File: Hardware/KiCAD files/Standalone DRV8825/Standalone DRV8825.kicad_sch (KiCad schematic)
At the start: 18 parts, among them J10 PINHD_1x8_Male, J9 PINHD_1x8_Male, U5 DRV8825PWPR

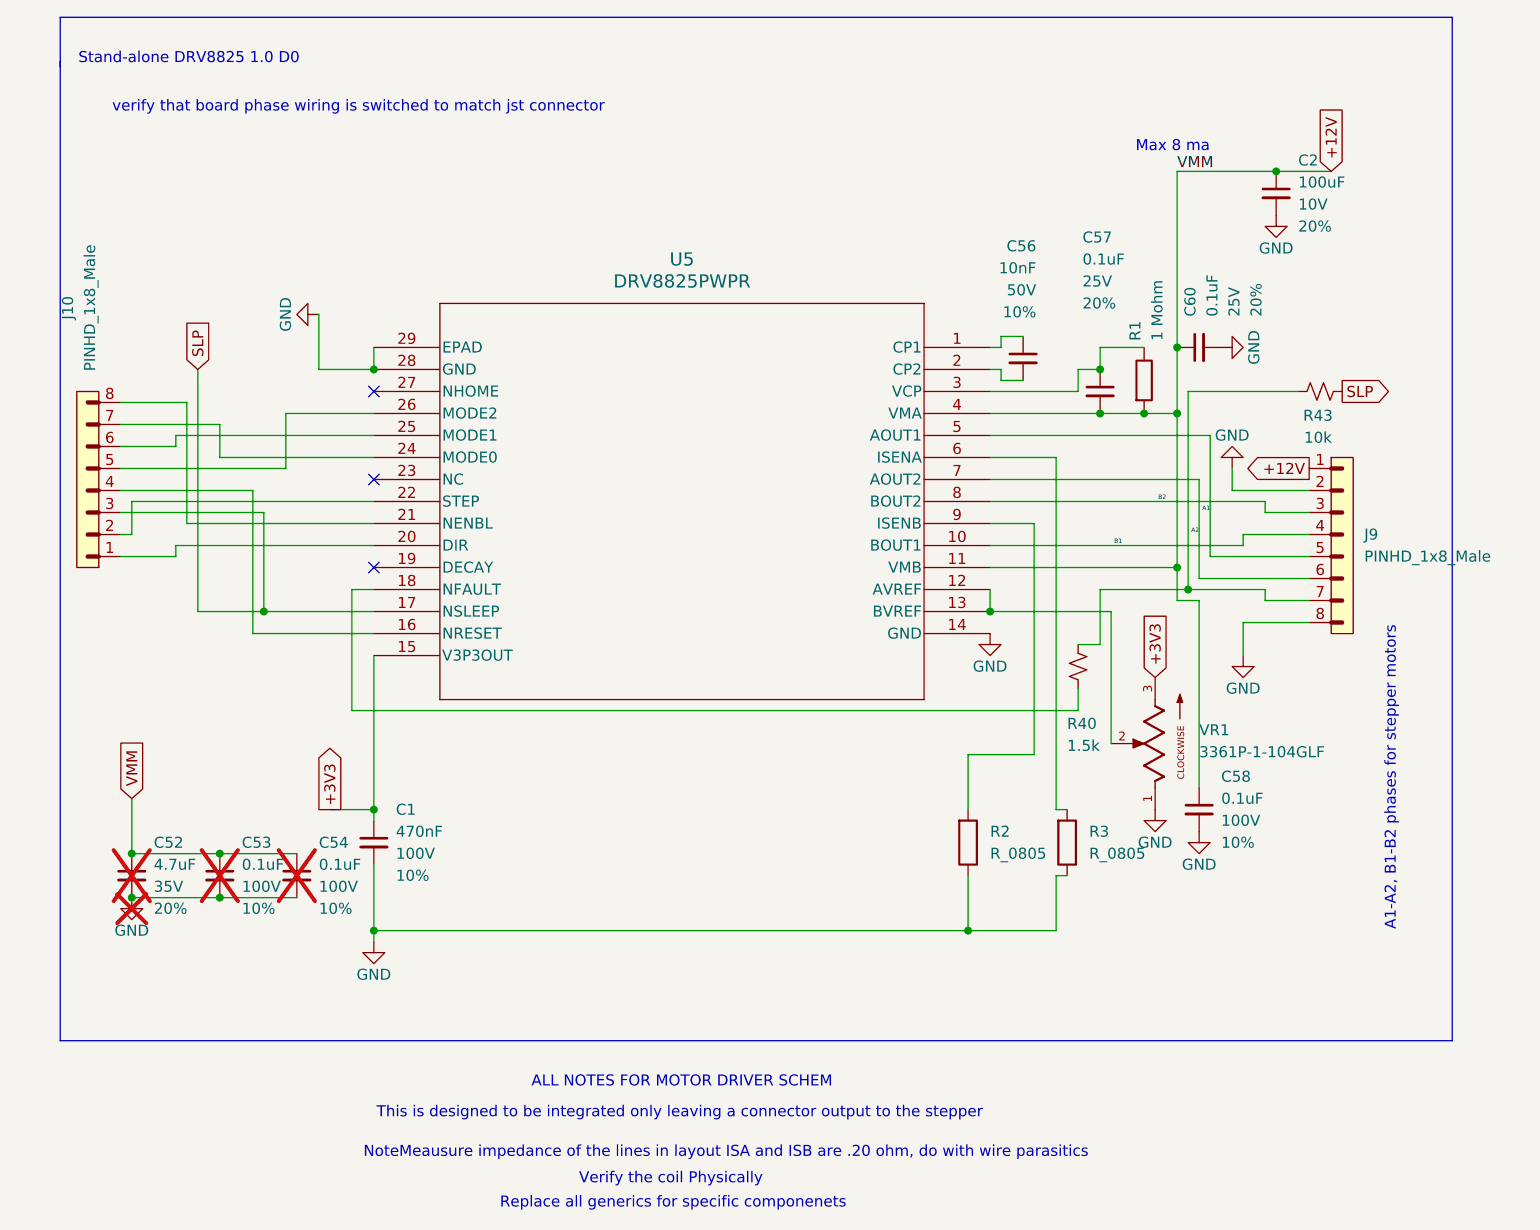
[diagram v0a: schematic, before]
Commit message: general progress and adjustments
new footprint for pi reg inductor, var reg checked concurred with current part and value. re footprinted motor driver. started swapping head. adjusted some device footprints.
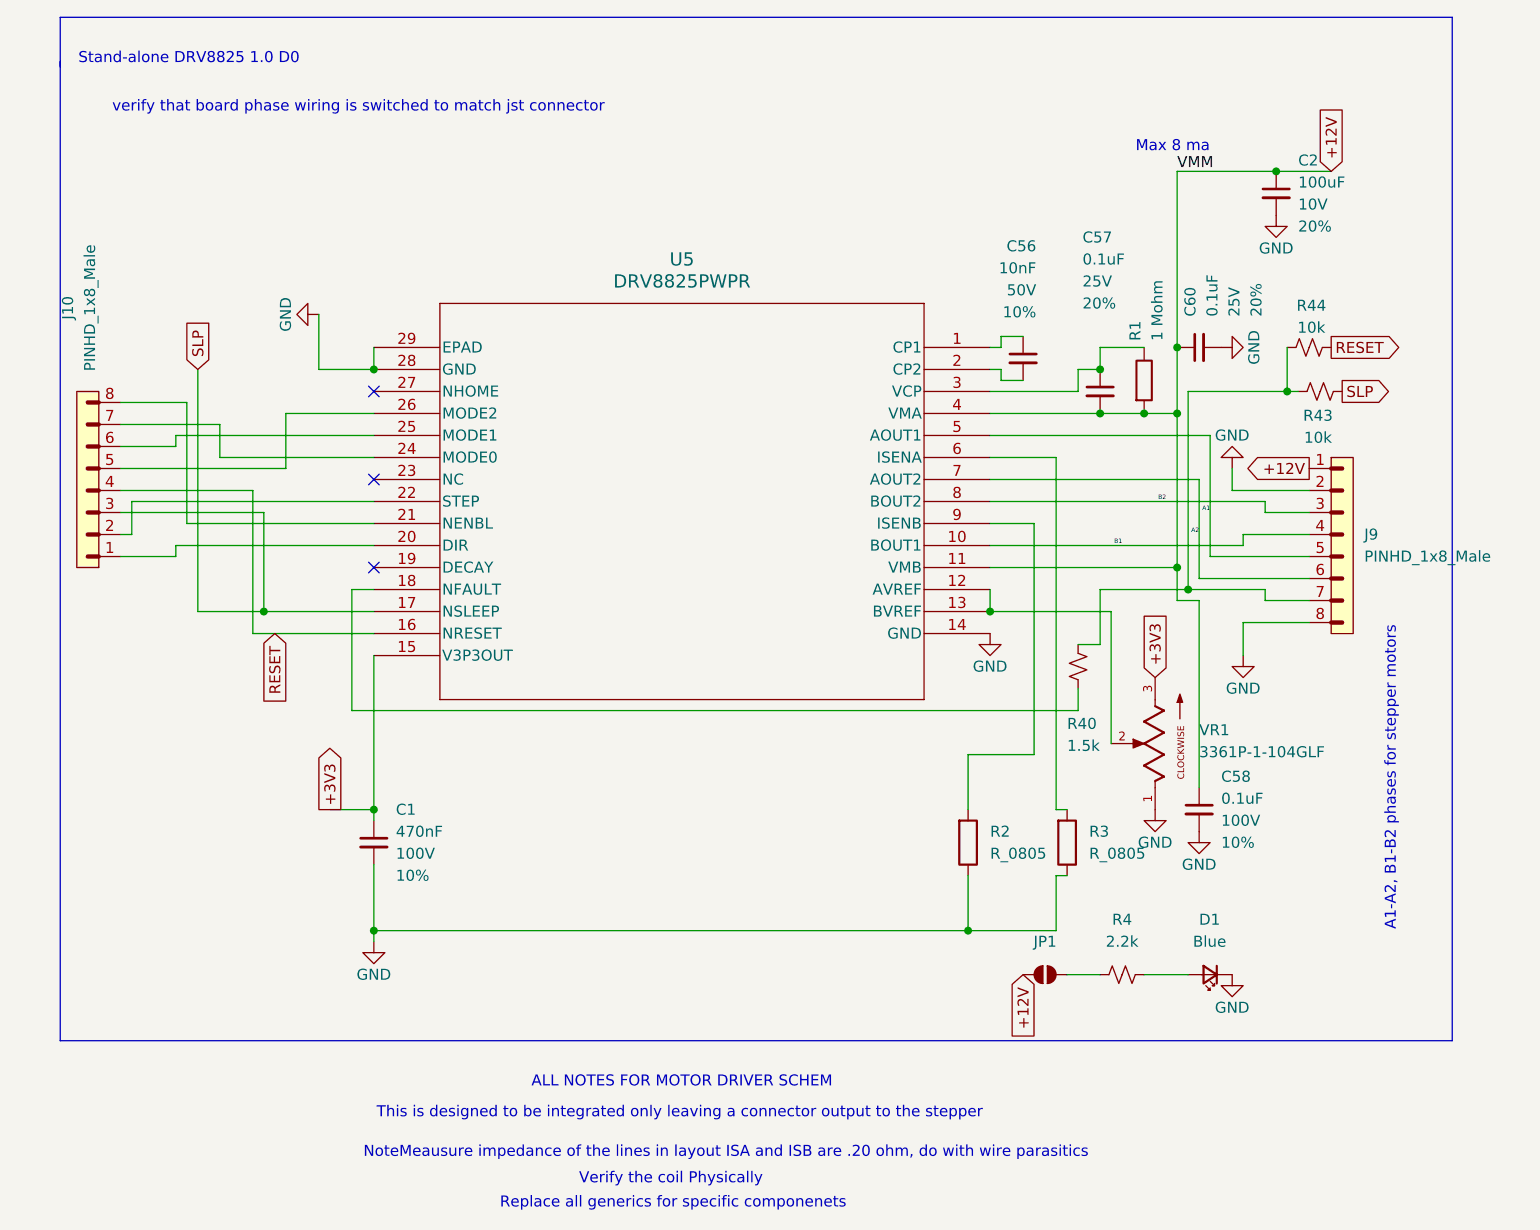
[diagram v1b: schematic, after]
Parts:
- removed C52: 4.7uF, PCM_SparkFun-Capacitor:C_0603_1608Metric, symbol PCM_SparkFun-Capacitor:4.7uF_0603_35V_20%
- removed C53, C54: 0.1uF, PCM_SparkFun-Capacitor:C_0603_1608Metric, symbol PCM_SparkFun-Capacitor:0.1uF_0603_100V_10%
- added D1: Blue, PCM_SparkFun-LED:LED_0603_1608Metric_Blue, symbol PCM_SparkFun-LED:LED_Blue_0603
- added JP1: (no value), PCM_SparkFun-Jumper:Jumper_2_NO, symbol PCM_SparkFun-Jumper:SolderJumper_2_Open
- added R4: 2.2k, PCM_SparkFun-Resistor:R_0603_1608Metric, symbol PCM_SparkFun-Resistor:2.2k_0603
- added R44: 10k, PCM_SparkFun-Resistor:R_0603_1608Metric, symbol PCM_SparkFun-Resistor:10k_0603
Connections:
- net +12V: now also JP1.1 (A)
- net GND: now also D1.1 (K)
- net RESET: now reaches J10.4, U5.16 (NRESET)
- net RESET: now also R44.2
- net at J9.7, R40.2, R43.1: now also R44.1
- new net: JP1.2 (B), R4.1
- new net: D1.2 (A), R4.2

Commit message: general updates to the schematics and layouts
includes some backchecks tot he master schematic to be accurate for the paper
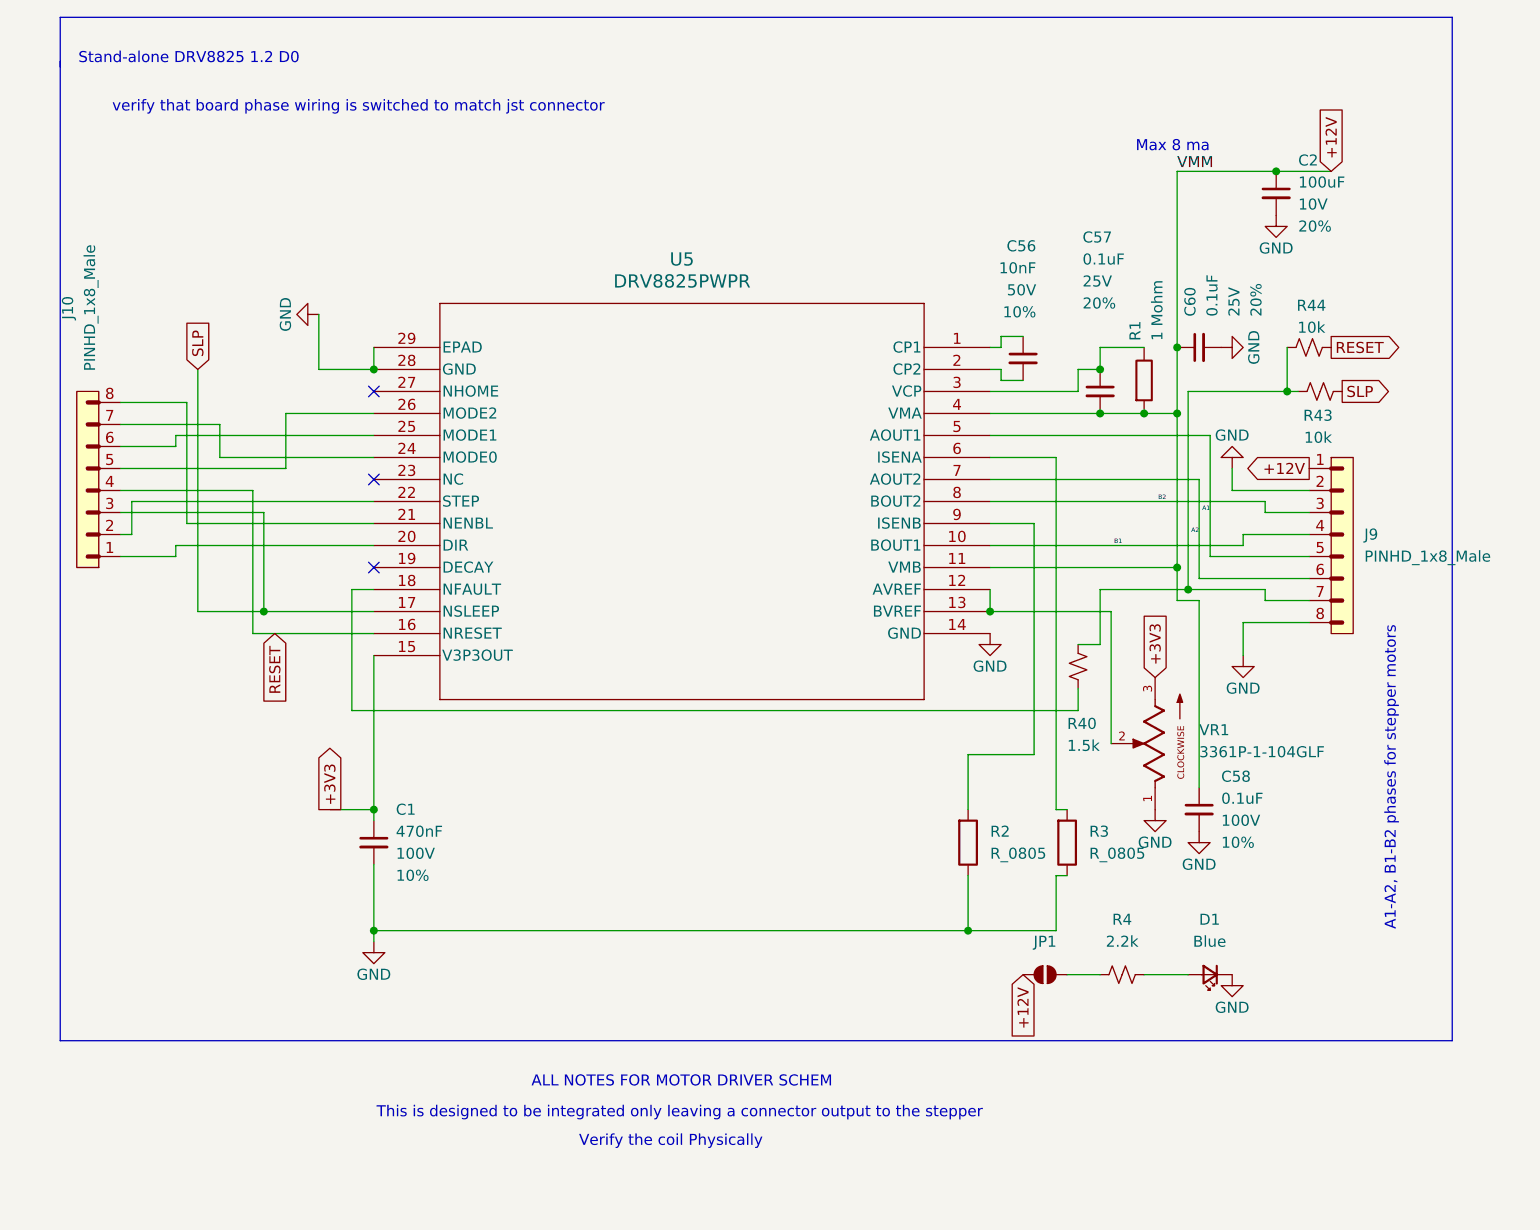
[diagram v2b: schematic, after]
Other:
- note added: "Stand-alone DRV8825 1.2 D0"
- note removed: "NoteMeausure impedance of the lines in layout ISA and ISB are .20 ohm, do with wire parasitics"
- note removed: "Replace all generics for specific componenets"
- note removed: "Stand-alone DRV8825 1.0 D0"
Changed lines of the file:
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@@
 	(generator_version "10.0")
 	(paper "A4")
-	(text "NoteMeausure impedance of the lines in layout ISA and ISB are .20 ohm, do with wire parasitics"
-		(exclude_from_sim no)
-		(at 146.05 148.844 0)
-		(effects
-			(font
-				(size 1.27 1.27)
-			)
-		)
-	)
 	(text "This is designed to be integrated only leaving a connector output to the stepper"
 		(exclude_from_sim no)
@@
 		(exclude_from_sim no)
 		(at 140.97 140.716 0)
-		(effects
-			(font
-				(size 1.27 1.27)
-			)
-		)
-	)
-	(text "Replace all generics for specific componenets\n"
-		(exclude_from_sim no)
-		(at 139.954 154.686 0)
 		(effects
 			(font
@@
 		)
 	)
-	(text "Stand-alone DRV8825 1.0 D0"
+	(text "Stand-alone DRV8825 1.2 D0"
 		(exclude_from_sim no)
 		(at 84.074 22.606 0)
@@
 	(text "Verify the coil Physically"
 		(exclude_from_sim no)
-		(at 139.7 151.892 0)
+		(at 139.7 147.574 0)
 		(effects
 			(font

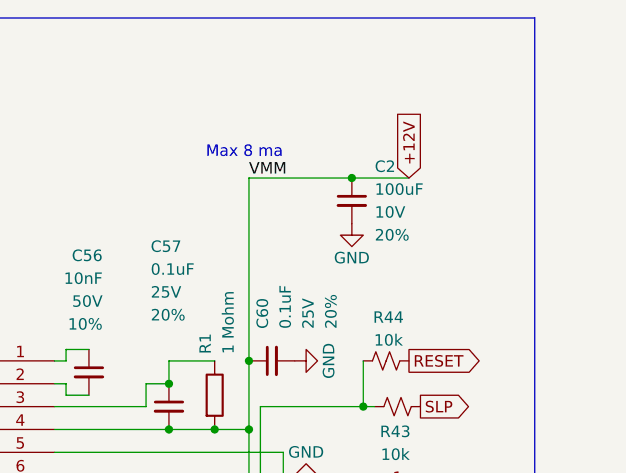
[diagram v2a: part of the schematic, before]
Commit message: part of the way through next iteration
Non-daisy chain Mainboard is ~50% through
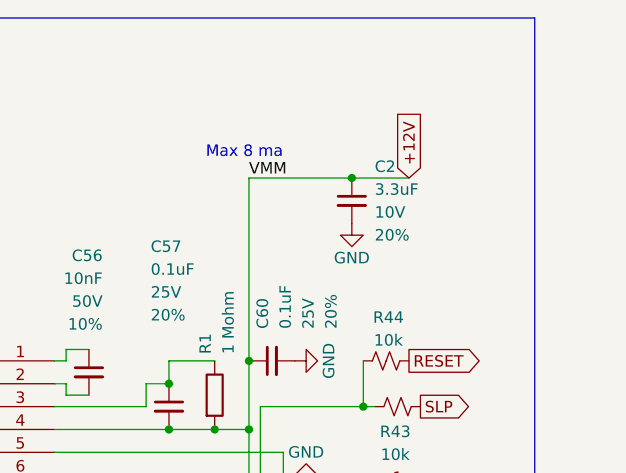
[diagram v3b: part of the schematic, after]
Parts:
- C2: value 100uF -> 3.3uF
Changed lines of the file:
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@@
 			)
 		)
-		(property "Value" "100uF"
+		(property "Value" "3.3uF"
 			(at 212.09 36.8362 0)
 			(show_name no)

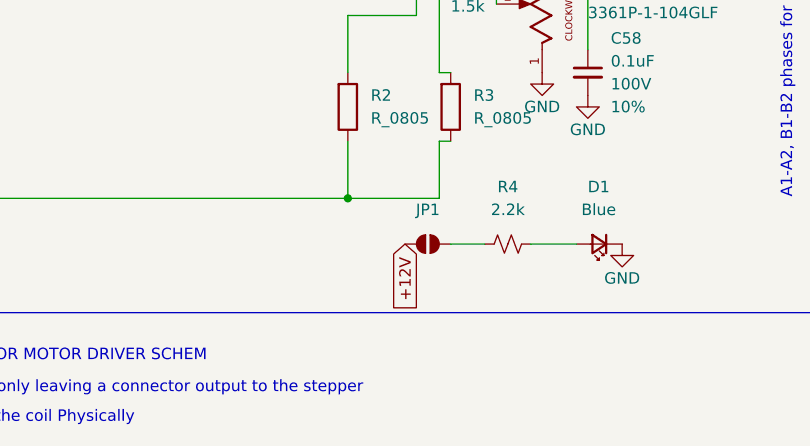
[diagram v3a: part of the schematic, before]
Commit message: 1st submitted iteration
added a folder for reviewing PCB's.
fixed various smaller issues on the PCB.
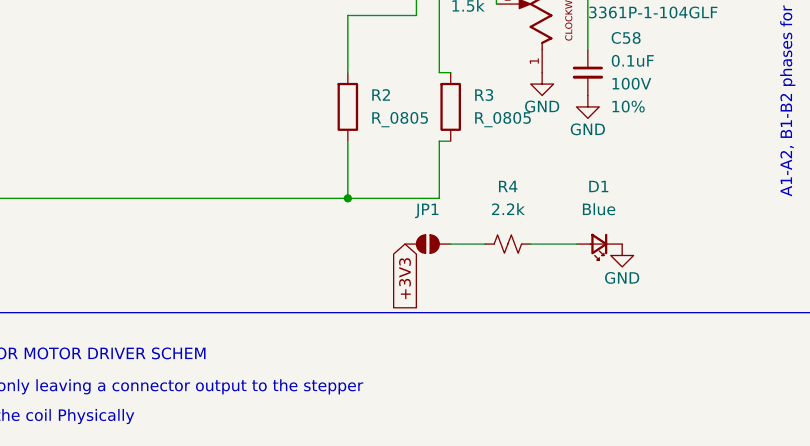
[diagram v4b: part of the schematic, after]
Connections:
- net +12V: no longer JP1.1 (A)
- net +3V3: now also JP1.1 (A)
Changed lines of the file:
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@@
 		)
 	)
-	(global_label "+12V"
+	(global_label "+3V3"
 		(shape input)
 		(at 180.34 128.27 270)

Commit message: sick weekend changes
small adjustments left our some larger protection changes till after talking to weeks
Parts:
- removed JP1: (no value), PCM_SparkFun-Jumper:Jumper_2_NO, symbol PCM_SparkFun-Jumper:SolderJumper_2_Open
- added R5: 0, Resistor_SMD:R_0805_2012Metric, symbol PCM_SparkFun-Resistor:2.2k_0603
- R4: footprint PCM_SparkFun-Resistor:R_0603_1608Metric -> Resistor_SMD:R_0805_2012Metric
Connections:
- net +3V3: now also R5.1
- net at R4.1: now also R5.2
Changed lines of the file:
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@@
 			)
 		)
-		(property "Footprint" "PCM_SparkFun-Resistor:R_0603_1608Metric"
+		(property "Footprint" "Resistor_SMD:R_0805_2012Metric"
 			(at 191.77 132.588 0)
 			(hide yes)
@@
 	)
 	(symbol
-		(lib_id "PCM_SparkFun-Jumper:SolderJumper_2_Open")
-		(at 182.88 128.27 0)
-		(unit 1)
-		(body_style 1)
-		(exclude_from_sim no)
-		(in_bom yes)
-		(on_board yes)
-		(in_pos_files yes)
-		(dnp no)
-		(fields_autoplaced yes)
-		(property "Reference" "JP1"
-			(at 182.88 124.46 0)
-			(show_name no)
-			(do_not_autoplace no)
-			(effects
-				(font
-					(size 1.27 1.27)
-				)
-			)
-		)
-		(property "Value" ""
-			(at 182.88 130.81 0)
-			(show_name no)
-			(do_not_autoplace no)
-			(effects
-				(font
-					(size 1.27 1.27)
-				)
-			)
-		)
-		(property "Footprint" "PCM_SparkFun-Jumper:Jumper_2_NO"
-			(at 182.88 131.572 0)
-			(hide yes)
-			(show_name no)
-			(do_not_autoplace no)
-			(effects
-				(font
-					(size 1.27 1.27)
-				)
-			)
-		)
-		(property "Datasheet" ""
-			(at 182.88 134.62 0)
-			(hide yes)
-			(show_name no)
-			(do_not_autoplace no)
-			(effects
-				(font
-					(size 1.27 1.27)
-				)
-			)
-		)
-		(property "Description" "Solder Jumper, 2-pole, open"
-			(at 182.88 137.16 0)
-			(hide yes)
-			(show_name no)
-			(do_not_autoplace no)
-			(effects
-				(font
-					(size 1.27 1.27)
-				)
-			)
-		)
-		(pin "1"
-		)
-		(pin "2"
-		)
-		(instances
-			(project "Standalone DRV8825"
-				(path "/f9c8590d-b7bb-4825-888e-ef9187573820"
-					(reference "JP1")
-					(unit 1)
-				)
-			)
-		)
-	)
-	(symbol
 		(lib_id "PCM_SparkFun-Capacitor:0.1uF_0603_100V_10%")
 		(at 200.66 109.22 0)
@@
 					(unit 1)
 				)
+			)
+		)
+	)
+	(symbol
+		(lib_id "PCM_SparkFun-Resistor:2.2k_0603")
+		(at 182.88 128.27 0)
+		(unit 1)
+		(body_style 1)
+		(exclude_from_sim no)
+		(in_bom yes)
+		(on_board yes)
+		(in_pos_files yes)
+		(dnp no)
+		(fields_autoplaced yes)
+		(property "Reference" "R5"
+			(at 182.88 121.92 0)
+			(show_name no)
+			(do_not_autoplace no)
+			(effects
+				(font
+					(size 1.27 1.27)
+				)
+			)
+		)
+		(property "Value" "0"
+			(at 182.88 124.46 0)
+			(show_name no)
+			(do_not_autoplace no)
+			(effects
+				(font
+					(size 1.27 1.27)
+				)
+			)
+		)
+		(property "Footprint" "Resistor_SMD:R_0805_2012Metric"
+			(at 182.88 132.588 0)
+			(hide yes)
+			(show_name no)
+			(do_not_autoplace no)
+			(effects
+				(font
+					(size 1.27 1.27)
+				)
+			)
+		)
+		(property "Datasheet" "https://www.vishay.com/docs/20035/dcrcwe3.pdf"
+			(at 182.88 137.16 0)
+			(hide yes)
+			(show_name no)
+			(do_not_autoplace no)
+			(effects
+				(font
+					(size 1.27 1.27)
+				)
+			)
+		)
+		(property "Description" "Resistor"
+			(at 182.88 139.7 0)
+			(hide yes)
+			(show_name no)
+			(do_not_autoplace no)
+			(effects
+				(font
+					(size 1.27 1.27)
+				)
+			)
+		)
+		(property "PROD_ID" "RES-08272"
+			(at 182.88 135.128 0)
+			(hide yes)
+			(show_name no)
+			(do_not_autoplace no)
+			(effects
+				(font
+					(size 1.27 1.27)
+				)
+			)
+		)
+		(pin "1"
+		)
+		(pin "2"
+		)
+		(instances
+			(project "Standalone DRV8825"
+				(path "/f9c8590d-b7bb-4825-888e-ef9187573820"
+					(reference "R5")
+					(unit 1)
+				)
